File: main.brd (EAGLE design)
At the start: 55 x 73 mm, 28 parts, among them U1 MCP2551P-SOCKET, U2 STN1110SOCKET-28, Y1 16Mhz

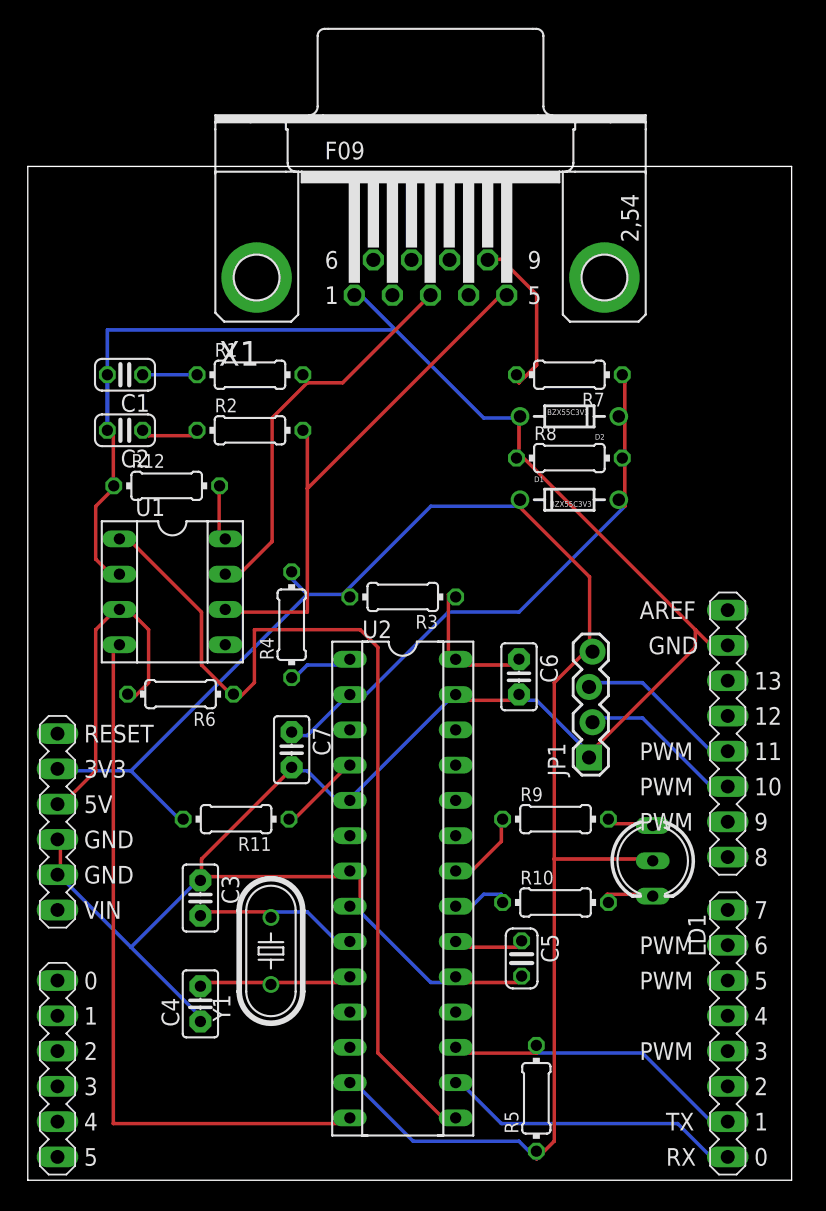
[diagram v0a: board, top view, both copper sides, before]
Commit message: Added some space and better routing
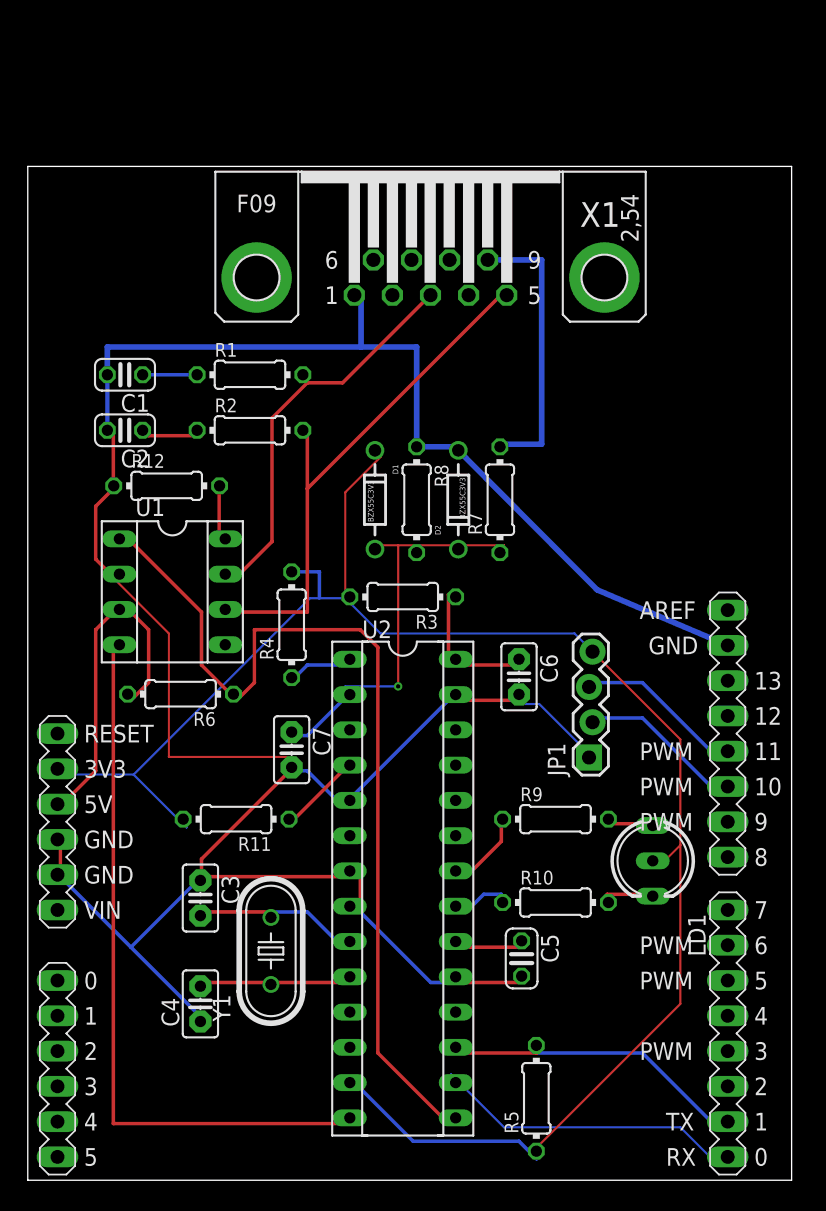
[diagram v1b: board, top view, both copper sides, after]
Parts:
- moved D1 14.0 mm to (25.0, 49.0), turned to 270 degrees
- moved R8 11.4 mm to (28.0, 49.0), turned to 270 degrees
- moved R7 10.3 mm to (34.0, 49.0), turned to 90 degrees
- moved D2 10.0 mm to (31.0, 49.0), turned to 90 degrees
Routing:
- net GND: track 189.1 -> 201.2 mm
- net ANALOG_IN: track 43.1 -> 32.0 mm, vias 0 -> 1
- net V_BATT: track 12.6 -> 20.6 mm
- net 3.3V: track 125.5 -> 129.7 mm
- net UART_RX: track 21.8 -> 23.3 mm

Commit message: Improved routing, added micro-sd slot
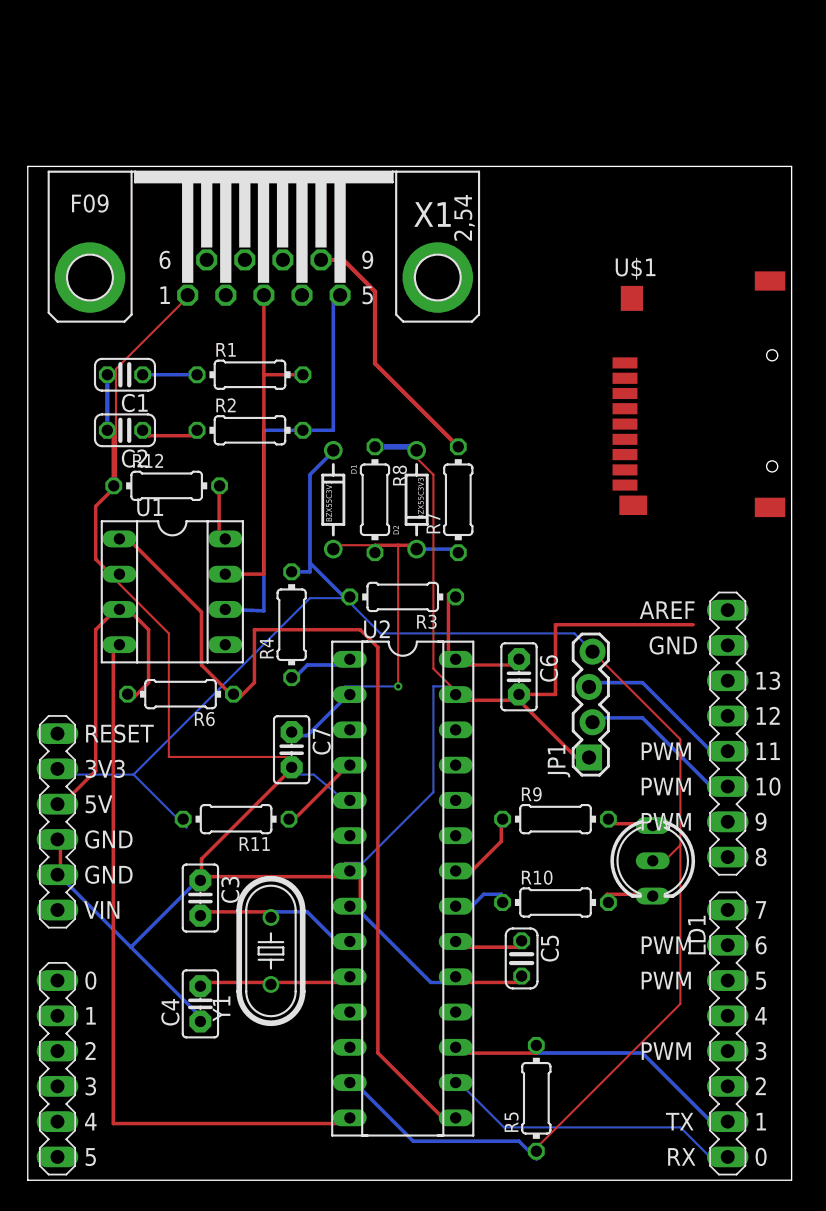
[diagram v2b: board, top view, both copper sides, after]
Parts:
- added U$1: MICROSD_PP, DE1594-v2:MICROSD_PP
- moved X1 12.0 mm to (17.0, 65.0)
- moved D1 3.00 mm to (22.0, 49.0)
- moved D2 3.00 mm to (28.0, 49.0)
- moved R7 3.00 mm to (31.0, 49.0)
- moved R8 3.00 mm to (25.0, 49.0)
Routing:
- net N$2: track 39.3 -> 31.0 mm
- net N$1: track 29.2 -> 25.7 mm
- net V_BATT: track 20.6 -> 18.5 mm
- net ANALOG_IN: track 32.0 -> 33.6 mm
- net 3.3V: track 129.7 -> 128.3 mm

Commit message: Wired the SD card and level shifter
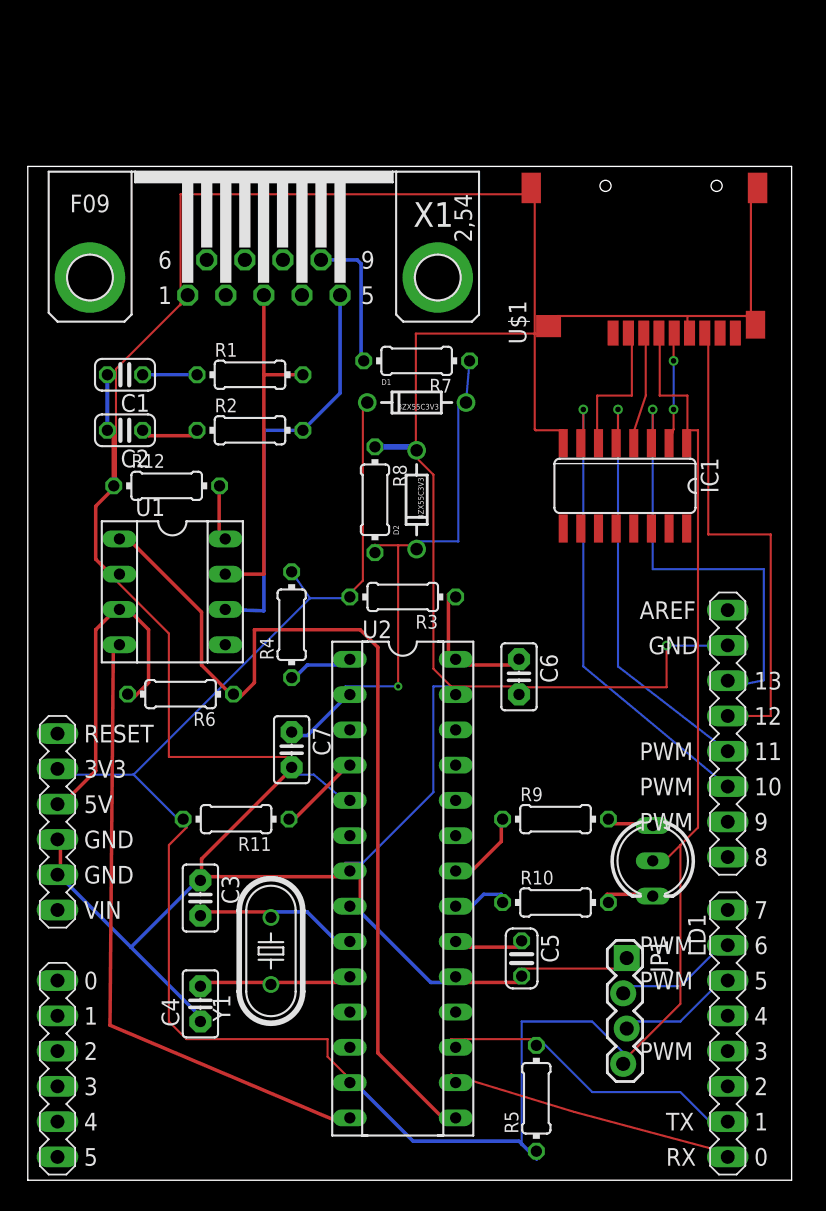
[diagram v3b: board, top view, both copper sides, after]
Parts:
- added IC1: 4050D, 40xx:SO16
- moved JP1 14.6 mm to (43.0, 16.0), turned to 270 degrees
- moved R7 10.4 mm to (28.0, 59.0), turned to 180 degrees
- moved D1 9.22 mm to (28.0, 56.0), turned to 0 degrees
- moved U$1 6.71 mm to (46.0, 61.0), turned to 90 degrees
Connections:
- new net N$13: IC1.4, U$1.3
- new net N$15: IC1.6, U$1.2
- new net N$16: ARDUINO1.13, IC1.3
- new net N$17: IC1.2, U$1.5
- new net N$18: ARDUINO1.10, IC1.7
- new net N$19: ARDUINO1.12, U$1.7
- new net N$20: ARDUINO1.11, IC1.5
- net 3.3V: now also IC1.1, U$1.4
- net GND: now also IC1.8, U$1.6, U$1.GND@1, U$1.GND@2, U$1.GND@3, U$1.GND@4
- net GPS_RX: now also ARDUINO1.05; no longer ARDUINO1.11
- net GPS_TX: now also ARDUINO1.06; no longer ARDUINO1.10
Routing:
- net GND: track 200.7 -> 302.6 mm, vias 0 -> 1
- net 3.3V: track 128.3 -> 176.4 mm
- net N$19: track 0.00 -> 35.4 mm
- net N$18: track 0.00 -> 34.6 mm, vias 0 -> 1
- net N$16: track 0.00 -> 32.6 mm, vias 0 -> 1
- net N$20: track 0.00 -> 31.0 mm, vias 0 -> 1
- net N$15: track 0.00 -> 10.6 mm
- net V_BATT: track 18.5 -> 10.1 mm
- net N$13: track 0.00 -> 8.26 mm
- net N$17: track 0.00 -> 8.03 mm, vias 0 -> 2
- net ANALOG_IN: track 33.6 -> 41.4 mm
- net CAN_RX: track 51.9 -> 46.5 mm
- net GPS_RX: track 12.4 -> 8.88 mm
- net GPS_TX: track 12.4 -> 8.96 mm
- net N$2: track 31.0 -> 29.4 mm
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
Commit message: fix missing board
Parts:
- removed LD1: (no value), led:DUOLED-A-5MM
- added JP2: 5V Transformer, SparkFun-Connectors:1X04_LOCK
- added LED1: L-115WEGW-CA, led:DUOLED-A-3MM
- U$1: value MICROSD_PP -> MICROSD
- moved C2 1.50 mm to (8.50, 54.0)
- moved C1 1.40 mm to (8.40, 58.0)
- moved R6 1.36 mm to (12.3, 34.6)
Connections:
- net 3.3V: now also LED1.2; no longer LD1.A
- net 5V: now also JP2.1
- net GND: now also JP2.2, JP2.3
- net N$10: now also LED1.1; no longer LD1.CX
- net N$11: now also LED1.3; no longer LD1.CR
- net V_BATT: now also JP2.4
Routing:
- net V_BATT: track 10.1 -> 46.6 mm
- net N$23: track 0.00 -> 14.7 mm
- net 5V: track 25.0 -> 33.9 mm
- net N$22: track 0.00 -> 5.00 mm
- net CAN_TX: track 68.0 -> 63.1 mm
- net GND: track 302.6 -> 298.7 mm
- net N$4: track 4.89 -> 3.47 mm
- net N$3: track 3.92 -> 2.52 mm
- net ANALOG_IN: track 41.4 -> 42.2 mm
- net N$16: track 32.6 -> 32.0 mm

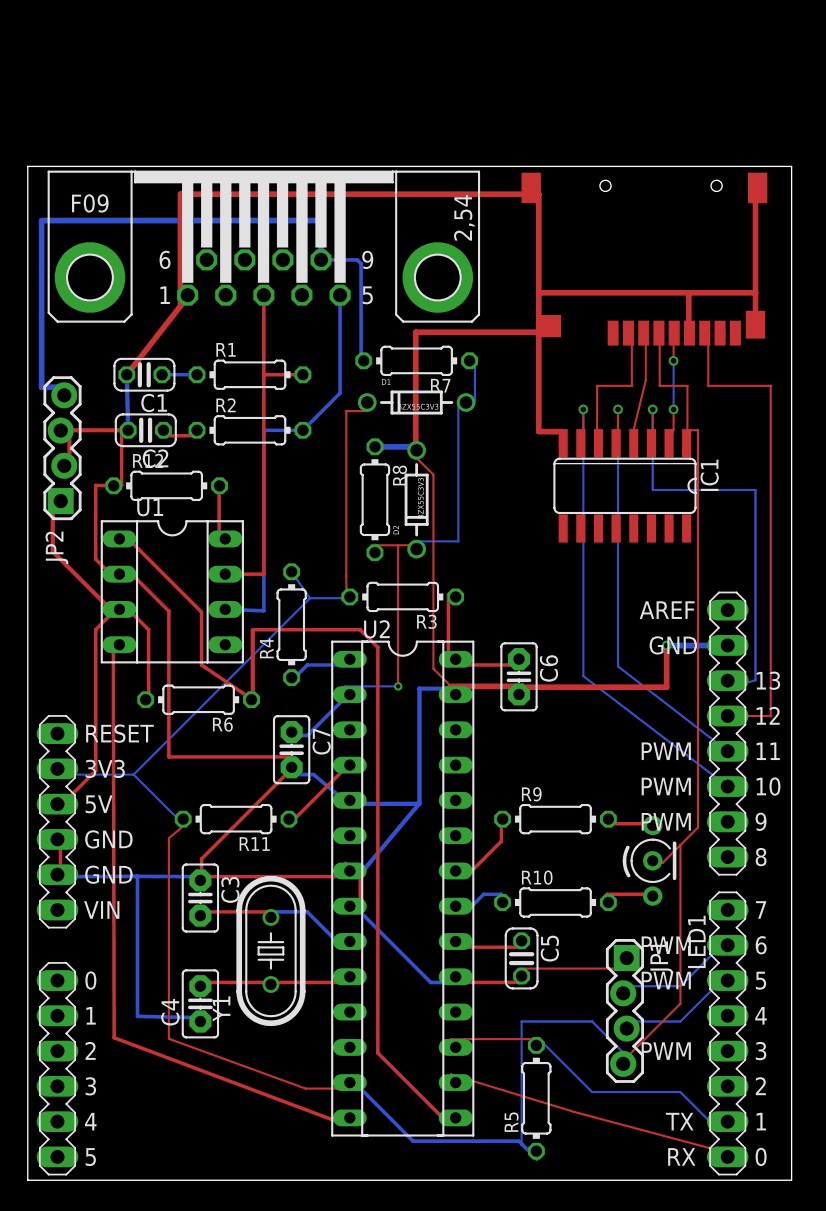
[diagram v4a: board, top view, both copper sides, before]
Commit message: Reduced footprint, fixed DB9 connector
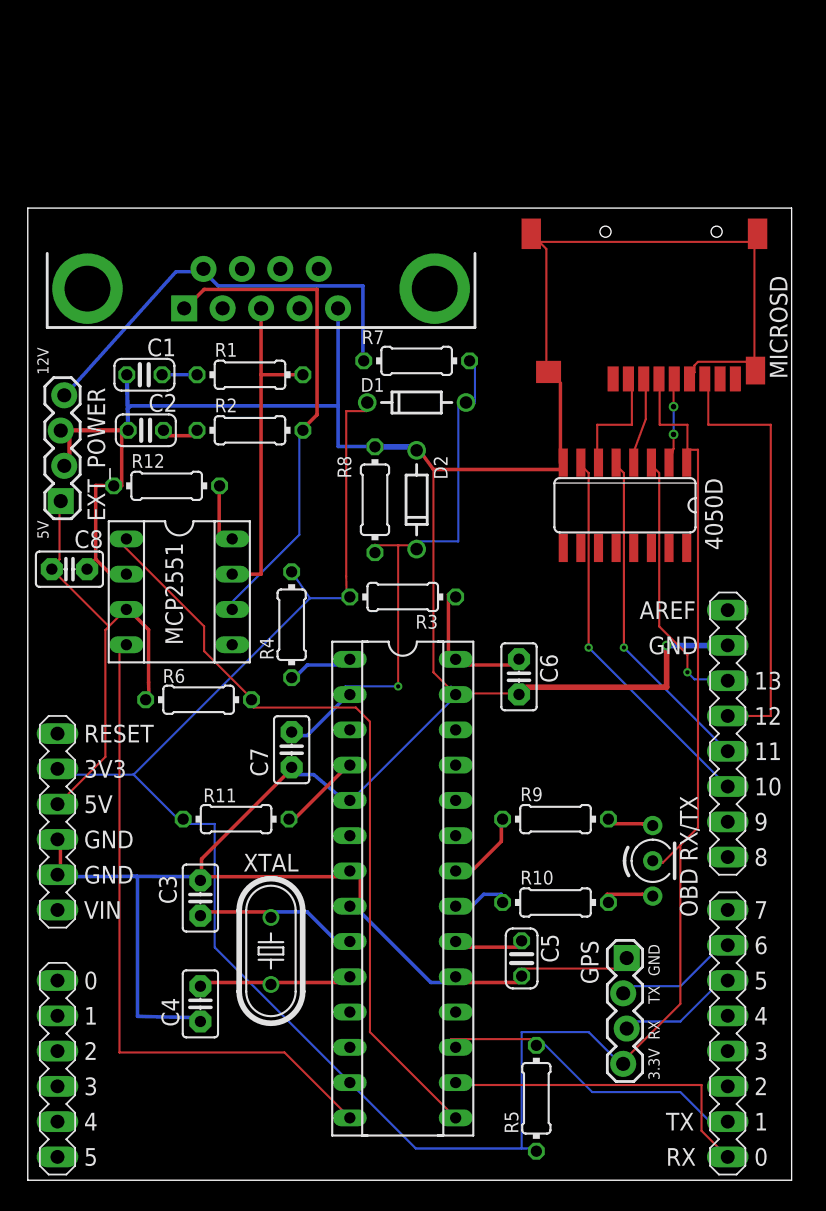
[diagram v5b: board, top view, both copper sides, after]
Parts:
- added C8: 0.1uF, capacitor-wima:C2.5-2
- LED1: value L-115WEGW-CA -> OBD RX/TX
- U1: value MCP2551P-SOCKET -> MCP2551
- U2: value STN1110SOCKET-28 -> STN1110
- X1: device con-subd:F09HP -> SparkFun-Connectors:DB9_MALE
- moved U$1 3.30 mm to (46.0, 57.7)
- moved IC1 1.40 mm to (43.0, 48.6)
- moved X1 0.82 mm to (16.8, 64.2)
- moved U1 0.50 mm to (10.9, 42.4)
- renumbered JP2 to EXT_POWER, Y1 to XTAL
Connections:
- net 5V: now also C8.1
- net GND: now also C8.2
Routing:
- net GND: track 298.7 -> 258.2 mm
- net V_BATT: track 46.6 -> 31.5 mm
- net N$23: track 14.7 -> 0.00 mm
- net N$16: track 32.0 -> 19.3 mm
- net 3.3V: track 176.3 -> 165.4 mm
- net N$18: track 34.9 -> 27.7 mm
- net N$2: track 29.4 -> 36.4 mm
- net N$20: track 31.0 -> 24.1 mm
- net CAN_TX: track 63.1 -> 56.4 mm
- net N$22: track 5.00 -> 0.00 mm
- net N$19: track 35.4 -> 32.1 mm
- net N$17: track 8.03 -> 6.13 mm
- net N$15: track 10.6 -> 8.73 mm
- net N$13: track 8.22 -> 6.38 mm
- net UART_RX: track 22.1 -> 23.7 mm
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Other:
- board size 55 x 73 mm -> 55 x 70 mm
- board text added: "12V"
- board text added: "3.3V"
- board text added: "5V"
- board text added: "GND"
- board text added: "RX"
- board text added: "TX"

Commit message: Resized and ready for printing
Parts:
- added U$2: (no value), SparkFun-Aesthetics:OSHW-LOGO-S
- moved U$1 1.80 mm to (44.7, 56.4)
- moved C8 1.58 mm to (2.50, 42.5), turned to 90 degrees
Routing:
- net 3.3V: track 165.4 -> 155.2 mm, vias 0 -> 2
- net N$19: track 32.1 -> 24.2 mm
- net GND: track 258.2 -> 262.5 mm
- net N$15: track 8.73 -> 5.12 mm
- net 5V: track 34.5 -> 35.8 mm
- net N$13: track 6.38 -> 5.03 mm
- net N$17: track 6.13 -> 5.22 mm, vias 2 -> 0
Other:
- board size 55 x 70 mm -> 53.3 x 68.6 mm
- board text added: "OBD Logger shield V1"
